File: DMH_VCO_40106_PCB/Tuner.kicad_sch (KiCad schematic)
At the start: 34 parts, among them J11 AVR-ISP-6, SW3 SW_SPDT_321_OnOff, U5 ATtiny4313-P, U6 SM420561N

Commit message: Component placement ongoing
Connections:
- net at R66.1: now also U5.2 (PD0); no longer U5.9 (PD5)
- net at R60.1: now also U5.4 (PA1/XTAL2); no longer U5.7 (PD3)
- net at R64.1: now also U5.6 (PD2); no longer U5.2 (PD0)
- net at U5.3 (PD1): now also R65.1; no longer R63.1
- net at R62.1: now also U5.8 (PD4); no longer U5.4 (PA1/XTAL2)
- net at U5.5 (PA0/XTAL1): now also R61.1; no longer R67.1
- new net: R63.1, U5.7 (PD3)
- new net: R67.1, U5.9 (PD5)
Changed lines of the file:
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@@
-	(wire
-		(pts
-			(xy 40.64 52.07) (xy 156.21 52.07)
-		)
-		(stroke
-			(width 0)
-			(type default)
-		)
-	)
 	(wire
 		(pts
@@
 	(wire
 		(pts
-			(xy 114.3 92.71) (xy 114.3 113.03)
+			(xy 109.22 92.71) (xy 109.22 100.33)
 		)
 		(stroke
@@
 	(wire
 		(pts
-			(xy 99.06 72.39) (xy 99.06 100.33)
+			(xy 99.06 72.39) (xy 99.06 105.41)
 		)
 		(stroke
@@
 	(wire
 		(pts
-			(xy 106.68 41.91) (xy 106.68 105.41)
+			(xy 99.06 54.61) (xy 43.18 54.61)
 		)
 		(stroke
@@
 	(wire
 		(pts
+			(xy 104.14 110.49) (xy 104.14 52.07)
+		)
+		(stroke
+			(width 0)
+			(type default)
+		)
+	)
+	(wire
+		(pts
 			(xy 142.24 171.45) (xy 129.54 171.45)
 		)
@@
 	(wire
 		(pts
+			(xy 78.74 102.87) (xy 106.68 102.87)
+		)
+		(stroke
+			(width 0)
+			(type default)
+		)
+	)
+	(wire
+		(pts
 			(xy 142.24 158.75) (xy 132.08 158.75)
 		)
@@
 	(wire
 		(pts
+			(xy 99.06 41.91) (xy 156.21 41.91)
+		)
+		(stroke
+			(width 0)
+			(type default)
+		)
+	)
+	(wire
+		(pts
 			(xy 83.82 130.81) (xy 83.82 177.8)
 		)
@@
 	(wire
 		(pts
-			(xy 114.3 92.71) (xy 156.21 92.71)
-		)
-		(stroke
-			(width 0)
-			(type default)
-		)
-	)
-	(wire
-		(pts
-			(xy 101.6 102.87) (xy 78.74 102.87)
+			(xy 109.22 92.71) (xy 156.21 92.71)
 		)
 		(stroke
@@
 	(wire
 		(pts
-			(xy 104.14 54.61) (xy 43.18 54.61)
-		)
-		(stroke
-			(width 0)
-			(type default)
-		)
-	)
-	(wire
-		(pts
 			(xy 149.86 120.65) (xy 152.4 120.65)
 		)
@@
 	(wire
 		(pts
-			(xy 40.64 52.07) (xy 40.64 87.63)
+			(xy 40.64 57.15) (xy 40.64 87.63)
 		)
 		(stroke
@@
 	(wire
 		(pts
-			(xy 109.22 31.75) (xy 156.21 31.75)
-		)
-		(stroke
-			(width 0)
-			(type default)
-		)
-	)
-	(wire
-		(pts
-			(xy 111.76 82.55) (xy 156.21 82.55)
+			(xy 101.6 31.75) (xy 156.21 31.75)
+		)
+		(stroke
+			(width 0)
+			(type default)
+		)
+	)
+	(wire
+		(pts
+			(xy 106.68 82.55) (xy 156.21 82.55)
 		)
 		(stroke
@@
 	(wire
 		(pts
-			(xy 99.06 100.33) (xy 78.74 100.33)
-		)
-		(stroke
-			(width 0)
-			(type default)
-		)
-	)
-	(wire
-		(pts
-			(xy 106.68 41.91) (xy 156.21 41.91)
-		)
-		(stroke
-			(width 0)
-			(type default)
-		)
-	)
-	(wire
-		(pts
 			(xy 99.06 72.39) (xy 156.21 72.39)
 		)
@@
 	(wire
 		(pts
-			(xy 104.14 102.87) (xy 104.14 54.61)
+			(xy 109.22 102.87) (xy 109.22 113.03)
 		)
 		(stroke
@@
 	(wire
 		(pts
+			(xy 78.74 110.49) (xy 104.14 110.49)
+		)
+		(stroke
+			(width 0)
+			(type default)
+		)
+	)
+	(wire
+		(pts
 			(xy 86.36 92.71) (xy 78.74 92.71)
 		)
@@
 	(wire
 		(pts
-			(xy 111.76 110.49) (xy 78.74 110.49)
-		)
-		(stroke
-			(width 0)
-			(type default)
-		)
-	)
-	(wire
-		(pts
 			(xy 162.56 171.45) (xy 162.56 187.96)
 		)
@@
 	(wire
 		(pts
+			(xy 99.06 105.41) (xy 78.74 105.41)
+		)
+		(stroke
+			(width 0)
+			(type default)
+		)
+	)
+	(wire
+		(pts
 			(xy 114.3 115.57) (xy 78.74 115.57)
 		)
@@
 	(wire
 		(pts
+			(xy 99.06 41.91) (xy 99.06 54.61)
+		)
+		(stroke
+			(width 0)
+			(type default)
+		)
+	)
+	(wire
+		(pts
 			(xy 194.31 77.47) (xy 194.31 78.74)
 		)
@@
 	(wire
 		(pts
-			(xy 109.22 31.75) (xy 109.22 107.95)
-		)
-		(stroke
-			(width 0)
-			(type default)
-		)
-	)
-	(wire
-		(pts
 			(xy 45.72 152.4) (xy 81.28 152.4)
 		)
@@
 	(wire
 		(pts
-			(xy 114.3 113.03) (xy 78.74 113.03)
-		)
-		(stroke
-			(width 0)
-			(type default)
-		)
-	)
-	(wire
-		(pts
 			(xy 127 187.96) (xy 162.56 187.96)
 		)
@@
 	(wire
 		(pts
-			(xy 104.14 102.87) (xy 156.21 102.87)
+			(xy 109.22 102.87) (xy 156.21 102.87)
 		)
 		(stroke
@@
 	(wire
 		(pts
+			(xy 78.74 100.33) (xy 109.22 100.33)
+		)
+		(stroke
+			(width 0)
+			(type default)
+		)
+	)
+	(wire
+		(pts
 			(xy 134.62 125.73) (xy 88.9 125.73)
 		)
@@
 	(wire
 		(pts
-			(xy 111.76 82.55) (xy 111.76 110.49)
+			(xy 106.68 82.55) (xy 106.68 102.87)
 		)
 		(stroke
@@
 	(wire
 		(pts
+			(xy 101.6 62.23) (xy 101.6 107.95)
+		)
+		(stroke
+			(width 0)
+			(type default)
+		)
+	)
+	(wire
+		(pts
 			(xy 25.4 128.27) (xy 63.5 128.27)
 		)
@@
 	(wire
 		(pts
-			(xy 106.68 105.41) (xy 78.74 105.41)
-		)
-		(stroke
-			(width 0)
-			(type default)
-		)
-	)
-	(wire
-		(pts
-			(xy 109.22 107.95) (xy 78.74 107.95)
+			(xy 78.74 107.95) (xy 101.6 107.95)
 		)
 		(stroke
@@
 	(wire
 		(pts
+			(xy 40.64 57.15) (xy 101.6 57.15)
+		)
+		(stroke
+			(width 0)
+			(type default)
+		)
+	)
+	(wire
+		(pts
 			(xy 162.56 187.96) (xy 165.1 187.96)
 		)
@@
 	(wire
 		(pts
+			(xy 104.14 52.07) (xy 156.21 52.07)
+		)
+		(stroke
+			(width 0)
+			(type default)
+		)
+	)
+	(wire
+		(pts
 			(xy 173.99 80.01) (xy 175.26 80.01)
 		)
@@
 	(wire
 		(pts
+			(xy 101.6 31.75) (xy 101.6 57.15)
+		)
+		(stroke
+			(width 0)
+			(type default)
+		)
+	)
+	(wire
+		(pts
 			(xy 127 175.26) (xy 127 177.8)
 		)
@@
 	(wire
 		(pts
-			(xy 101.6 62.23) (xy 101.6 102.87)
-		)
-		(stroke
+			(xy 78.74 113.03) (xy 109.22 113.03)
+		)
+		(stroke

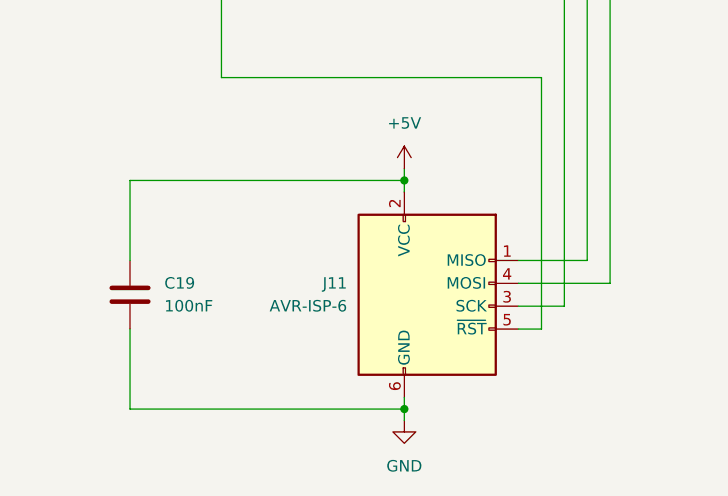
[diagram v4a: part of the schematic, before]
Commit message: Adjusted silk screen
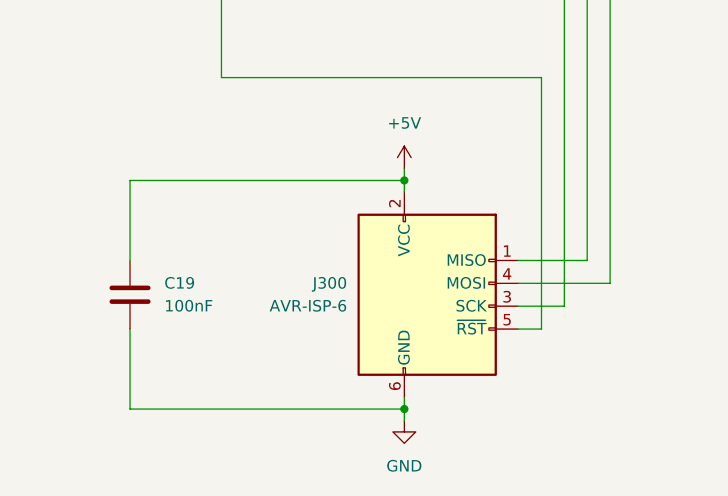
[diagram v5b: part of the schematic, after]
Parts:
- renumbered J11 to J300
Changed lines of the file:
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@@
 		(dnp no)
 		(fields_autoplaced yes)
-		(property "Reference" "J11"
+		(property "Reference" "J300"
 			(at 59.69 175.2599 0)
 			(effects
@@
 			(project ""
 				(path "/fefed352-c100-4617-bbfb-c55e7427b122/ec8b77a2-f589-4806-8224-6b0ccc79bab4"
-					(reference "J11")
+					(reference "J300")
 					(unit 1)
 				)

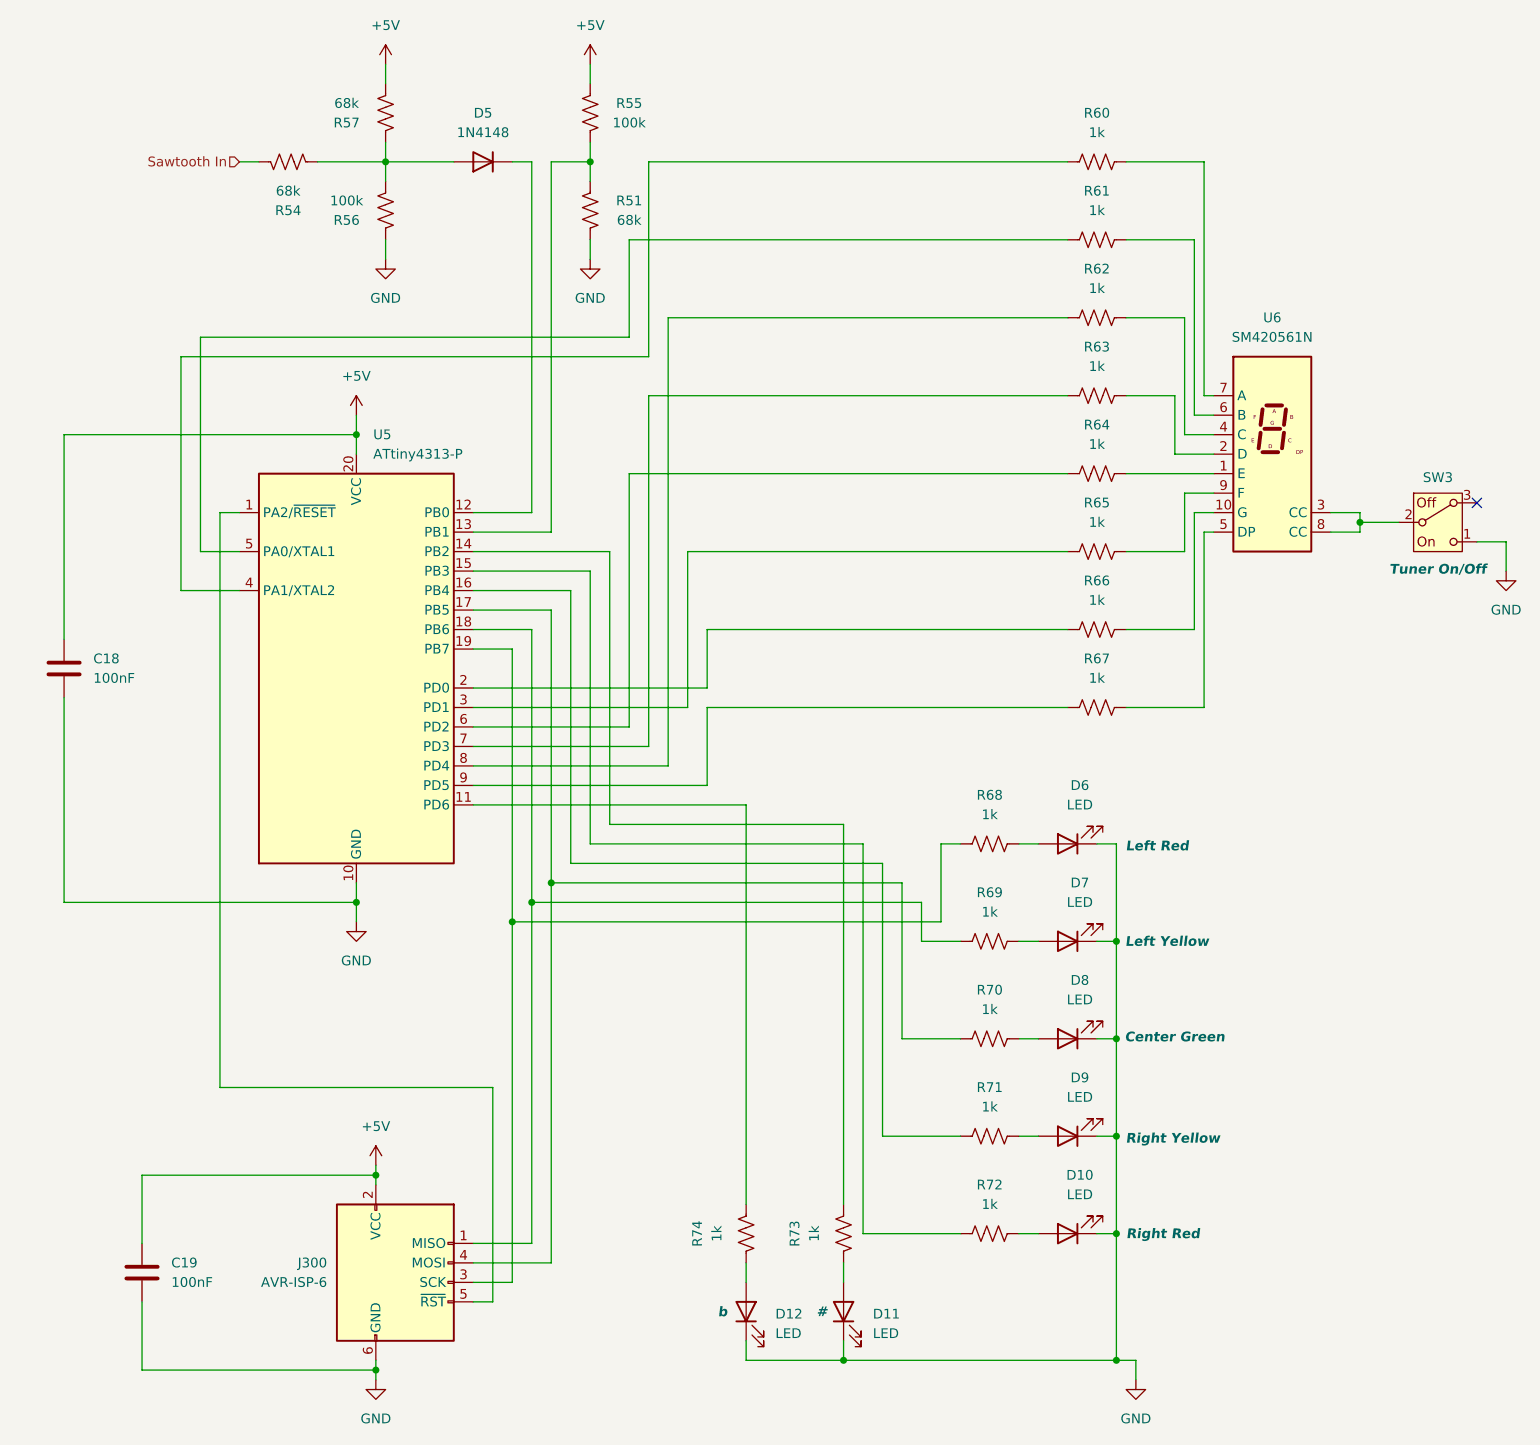
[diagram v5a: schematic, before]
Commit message: Removed the flat sign LED
and rerouted segments A and B to PORTD 6 and 7 respective,
and rerouted the DP segment to PORTA0
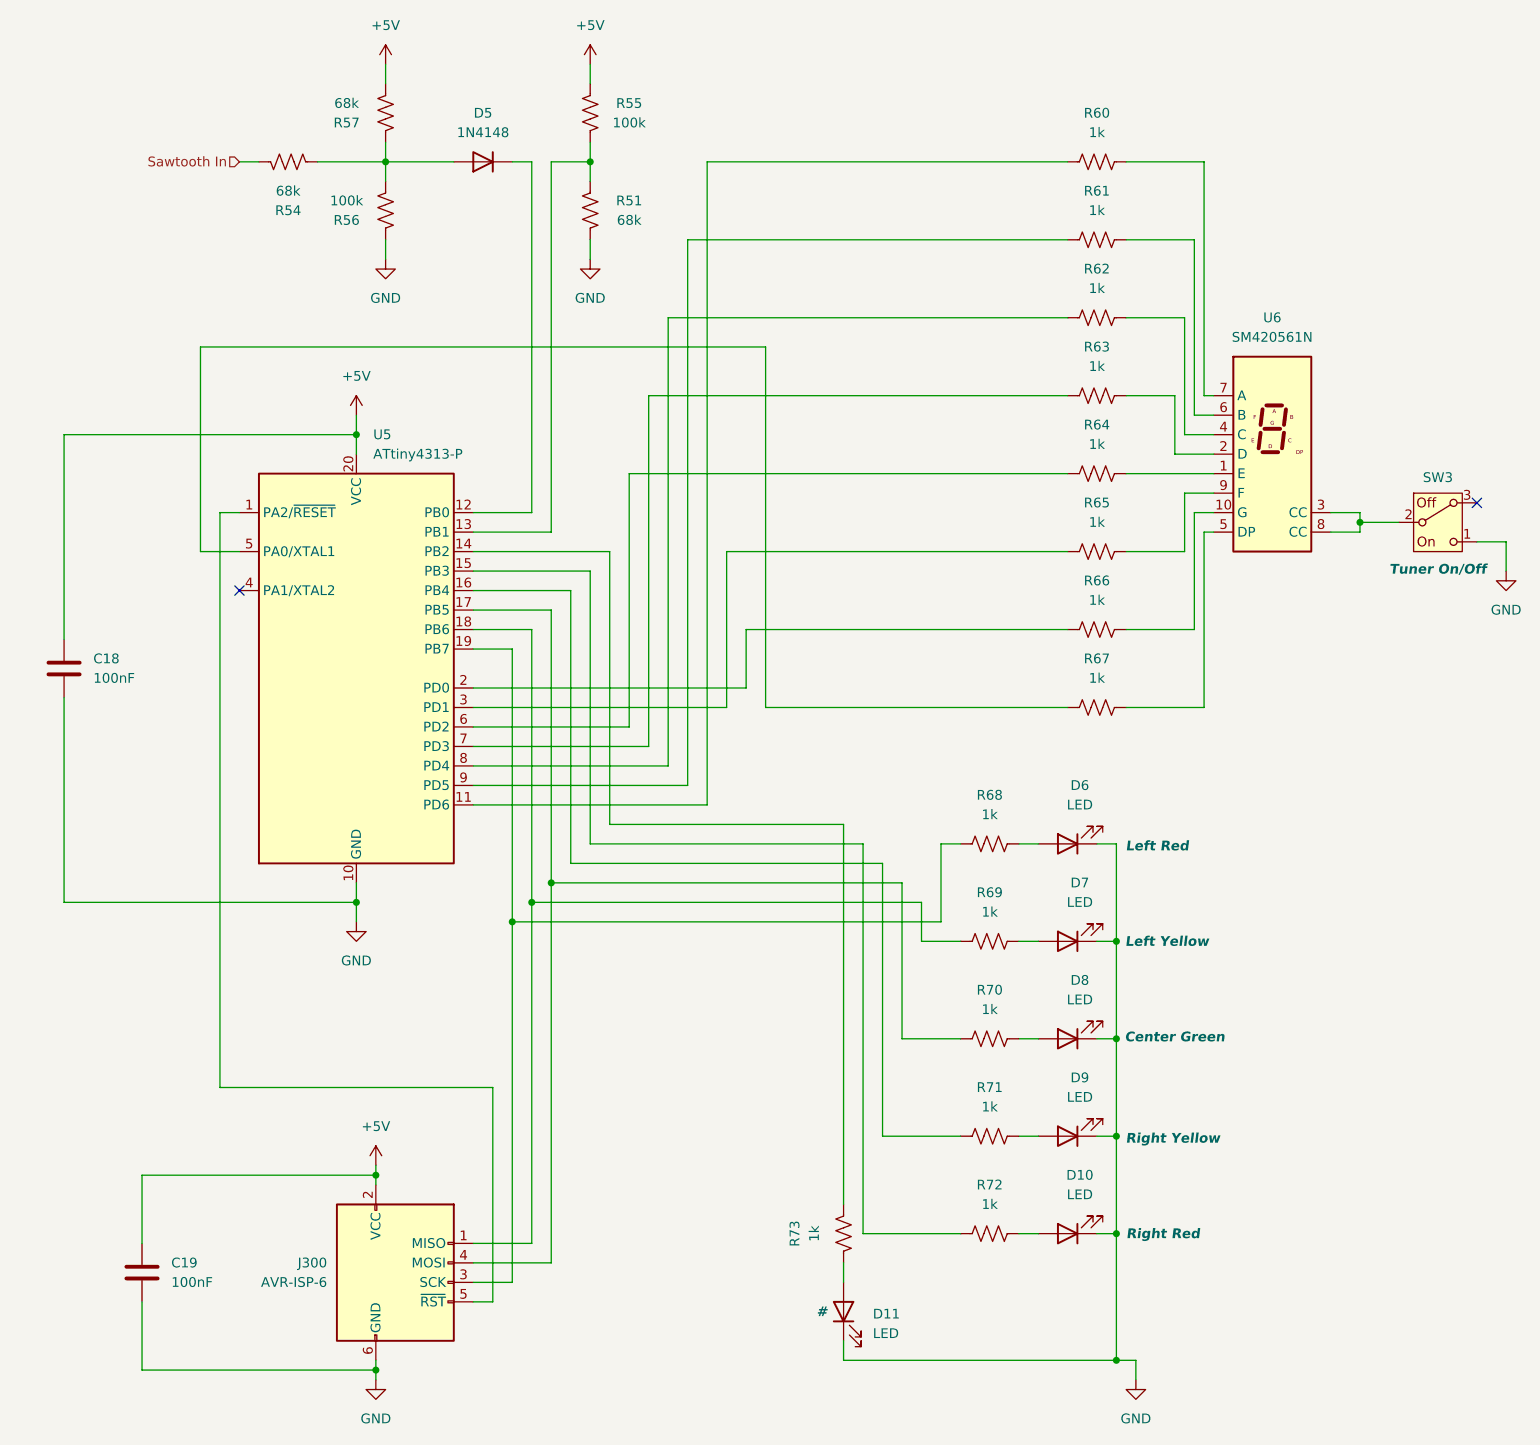
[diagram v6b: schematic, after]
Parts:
- removed D12: LED, LED_THT:LED_D3.0mm, symbol Device:LED
- removed R74: 1k, Resistor_THT:R_Axial_DIN0207_L6.3mm_D2.5mm_P7.62mm_Horizontal, symbol Device:R_US
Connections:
- net at R60.1: now also U5.11 (PD6); no longer U5.4 (PA1/XTAL2)
- net at U5.5 (PA0/XTAL1): now also R67.1; no longer R61.1
- net at U5.9 (PD5): now also R61.1; no longer R67.1
- no-connect marks 1 -> 2
